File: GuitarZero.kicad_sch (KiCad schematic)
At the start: 16 parts, among them J1 USB_A, J2 USB_B_Micro, J3 AudioJack3_SwitchT, SW1 SW_Push, SW2 SW_Push, SW3 SW_Push, SW4 SW_Push, SW5 SW_Push, SW6 SW_Push

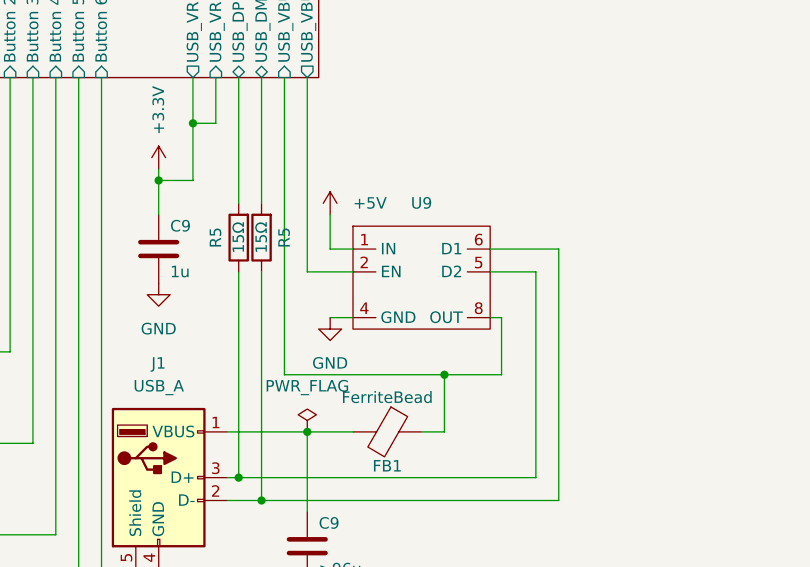
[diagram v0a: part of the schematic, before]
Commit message: Now follows with Electrical Rules
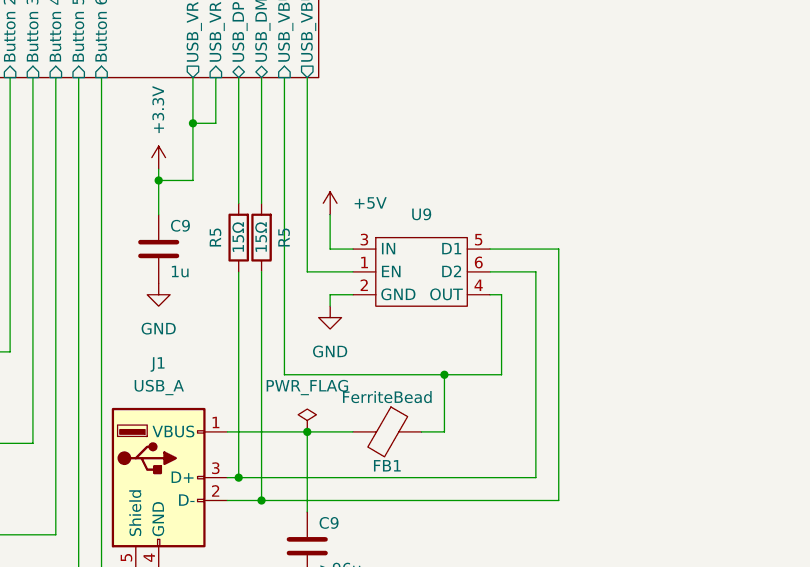
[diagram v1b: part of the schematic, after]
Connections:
- net +5V: now also U9.3 (IN); no longer U9.1 (IN)
- net GND: now also U9.2 (GND); no longer U9.4 (GND)
- net MCU/USB_VBUS: now also U9.4 (OUT); no longer U9.8 (OUT)
- net MCU/USB_VBUSEN: now also U9.1 (EN); no longer U9.2 (EN)
- net at J1.3 (D+), R5.1: now also U9.6 (D2); no longer U9.5 (D2)
- net at J1.2 (D-), R5.1: now also U9.5 (D1); no longer U9.6 (D1)

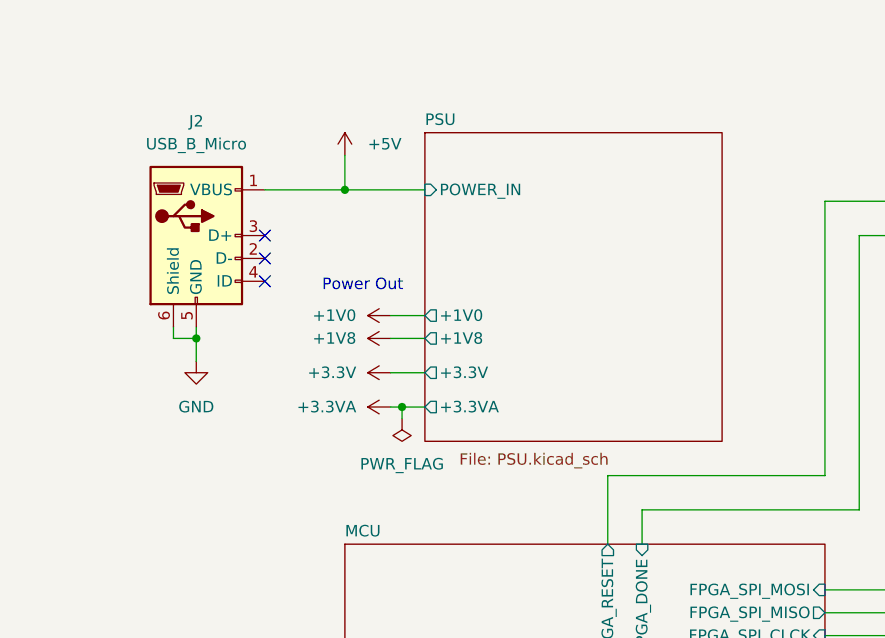
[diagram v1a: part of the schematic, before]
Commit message: Added PSU jumpers
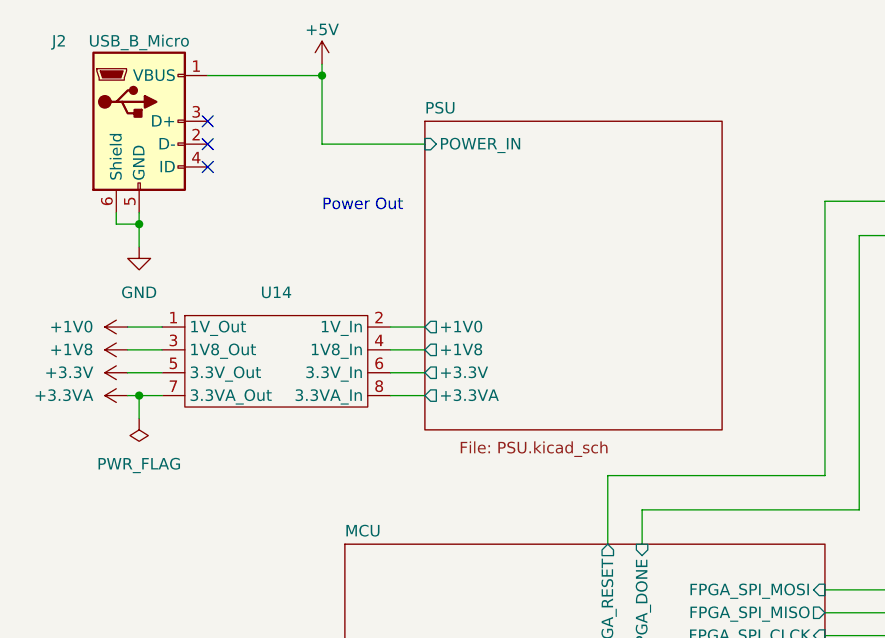
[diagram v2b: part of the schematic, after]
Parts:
- added U14: ~, symbol GuitarZero:PSU_Jumpers
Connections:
- net +1V0: now also U14.1 (1V_Out)
- net +1V8: now also U14.3 (1V8_Out)
- net +3.3V: now also U14.5 (3.3V_Out)
- net +3.3VA: now also U14.7 (3.3VA_Out)
- new net PSU/+1V0: U14.2 (1V_In)
- new net PSU/+1V8: U14.4 (1V8_In)
- new net PSU/+3.3V: U14.6 (3.3V_In)
- new net PSU/+3.3VA: U14.8 (3.3VA_In)
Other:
- moved on the sheet: J2

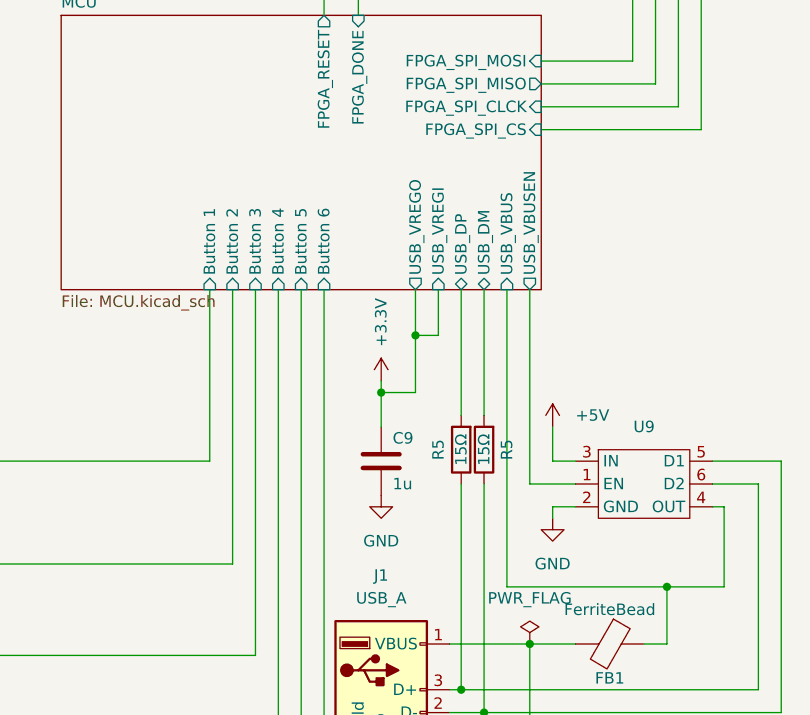
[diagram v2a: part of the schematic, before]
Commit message: Disconnected USB_VRGEI/O in root
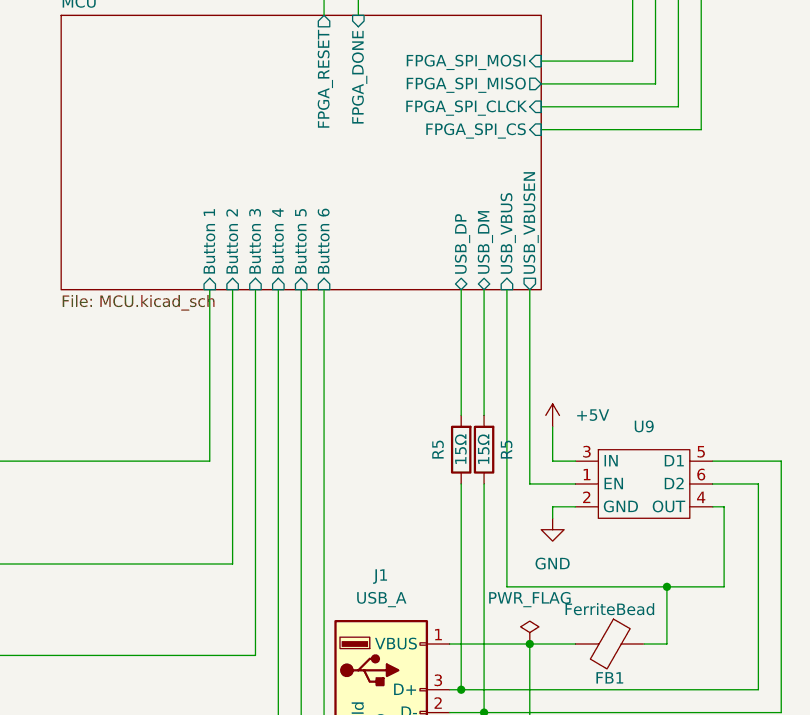
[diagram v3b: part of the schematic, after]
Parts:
- removed C9: 1u, symbol Device:C
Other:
- sheet MCU ports: added none; removed USB_VREGI, USB_VREGO
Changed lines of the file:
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@@
 (kicad_sch (version 20230121) (generator eeschema)
   (paper "A4")
-  (junction (at 82.55 113.03) (diameter 0) (color 0 0 0 0)
-  )
   (junction (at 232.41 25.4) (diameter 0) (color 0 0 0 0)
   )
@@
   )
   (junction (at 44.45 19.05) (diameter 0) (color 0 0 0 0)
-  )
-  (junction (at 86.36 106.68) (diameter 0) (color 0 0 0 0)
   )
   (junction (at 93.98 148.59) (diameter 0) (color 0 0 0 0)
@@
     (stroke (width 0) (type default))
   )
-  (wire (pts (xy 82.55 111.76) (xy 82.55 113.03))
-    (stroke (width 0) (type default))
-  )
   (wire (pts (xy 90.17 148.59) (xy 93.98 148.59))
     (stroke (width 0) (type default))
@@
     (stroke (width 0) (type default))
   )
-  (wire (pts (xy 86.36 101.6) (xy 86.36 106.68))
-    (stroke (width 0) (type default))
-  )
-  (wire (pts (xy 82.55 113.03) (xy 86.36 113.03))
-    (stroke (width 0) (type default))
-  )
   (wire (pts (xy 170.18 71.12) (xy 184.15 71.12))
     (stroke (width 0) (type default))
@@
     (stroke (width 0) (type default))
   )
-  (wire (pts (xy 86.36 106.68) (xy 88.9 106.68))
-    (stroke (width 0) (type default))
-  )
   (wire (pts (xy 237.49 25.4) (xy 232.41 25.4))
     (stroke (width 0) (type default))
@@
     (stroke (width 0) (type default))
   )
-  (wire (pts (xy 82.55 116.84) (xy 82.55 113.03))
-    (stroke (width 0) (type default))
-  )
   (wire (pts (xy 118.11 57.15) (xy 120.65 57.15))
     (stroke (width 0) (type default))
   )
-  (wire (pts (xy 86.36 113.03) (xy 86.36 106.68))
-    (stroke (width 0) (type default))
-  )
   (wire (pts (xy 24.13 142.24) (xy 27.94 142.24))
     (stroke (width 0) (type default))
@@
   )
   (wire (pts (xy 24.13 142.24) (xy 24.13 152.4))
-    (stroke (width 0) (type default))
-  )
-  (wire (pts (xy 88.9 101.6) (xy 88.9 106.68))
     (stroke (width 0) (type default))
   )
@@
         (path "/fba50eda-8593-4456-af98-ff56fd418a76"
           (reference "#PWR046") (unit 1)
-        )
-      )
-    )
-  )
-  (symbol (lib_id "power:+3.3V") (at 82.55 111.76 0) (unit 1)
-    (in_bom yes) (on_board yes) (dnp no)
-    (property "Reference" "#PWR051" (at 82.55 115.57 0)
-      (effects (font (size 1.27 1.27)) hide)
-    )
-    (property "Value" "+3.3V" (at 82.55 107.95 90)
-      (effects (font (size 1.27 1.27)) (justify left))
-    )
-    (property "Footprint" "" (at 82.55 111.76 0)
-      (effects (font (size 1.27 1.27)) hide)
-    )
-    (property "Datasheet" "" (at 82.55 111.76 0)
-      (effects (font (size 1.27 1.27)) hide)
-    )
-    (pin "1")
-    (instances
-      (project "GuitarZero"
-        (path "/fba50eda-8593-4456-af98-ff56fd418a76"
-          (reference "#PWR051") (unit 1)
         )
       )
@@
     )
   )
-  (symbol (lib_id "power:GND") (at 82.55 124.46 0) (unit 1)
-    (in_bom yes) (on_board yes) (dnp no)
-    (property "Reference" "#PWR050" (at 82.55 130.81 0)
-      (effects (font (size 1.27 1.27)) hide)
-    )
-    (property "Value" "GND" (at 82.55 129.54 0)
-      (effects (font (size 1.27 1.27)))
-    )
-    (property "Footprint" "" (at 82.55 124.46 0)
-      (effects (font (size 1.27 1.27)) hide)
-    )
-    (property "Datasheet" "" (at 82.55 124.46 0)
-      (effects (font (size 1.27 1.27)) hide)
-    )
-    (pin "1")
-    (instances
-      (project "GuitarZero"
-        (path "/fba50eda-8593-4456-af98-ff56fd418a76"
-          (reference "#PWR050") (unit 1)
-        )
-      )
-    )
-  )
   (symbol (lib_id "power:+3.3VA") (at 22.86 54.61 90) (unit 1)
     (in_bom yes) (on_board yes) (dnp no)
@@
         (path "/fba50eda-8593-4456-af98-ff56fd418a76"
           (reference "U9") (unit 1)
-        )
-      )
-    )
-  )
-  (symbol (lib_id "Device:C") (at 82.55 120.65 0) (unit 1)
-    (in_bom yes) (on_board yes) (dnp no)
-    (property "Reference" "C9" (at 83.82 118.11 0)
-      (effects (font (size 1.27 1.27)) (justify left))
-    )
-    (property "Value" "1u" (at 83.82 123.19 0)
-      (effects (font (size 1.27 1.27)) (justify left))
-    )
-    (property "Footprint" "" (at 83.5152 124.46 0)
-      (effects (font (size 1.27 1.27)) hide)
-    )
-    (property "Datasheet" "~" (at 82.55 120.65 0)
-      (effects (font (size 1.27 1.27)) hide)
-    )
-    (pin "1")
-    (pin "2")
-    (instances
-      (project "GuitarZero"
-        (path "/fba50eda-8593-4456-af98-ff56fd418a76/2f5e5303-1176-466f-800a-96bac7c62873"
-          (reference "C9") (unit 1)
-        )
-        (path "/fba50eda-8593-4456-af98-ff56fd418a76"
-          (reference "C71") (unit 1)
         )
       )
@@
       (effects (font (size 1.27 1.27)) (justify right))
     )
-    (pin "USB_VREGO" output (at 86.36 101.6 270)
-      (effects (font (size 1.27 1.27)) (justify left))
-    )
-    (pin "USB_VREGI" input (at 88.9 101.6 270)
-      (effects (font (size 1.27 1.27)) (justify left))
-    )
     (pin "USB_DP" bidirectional (at 91.44 101.6 270)

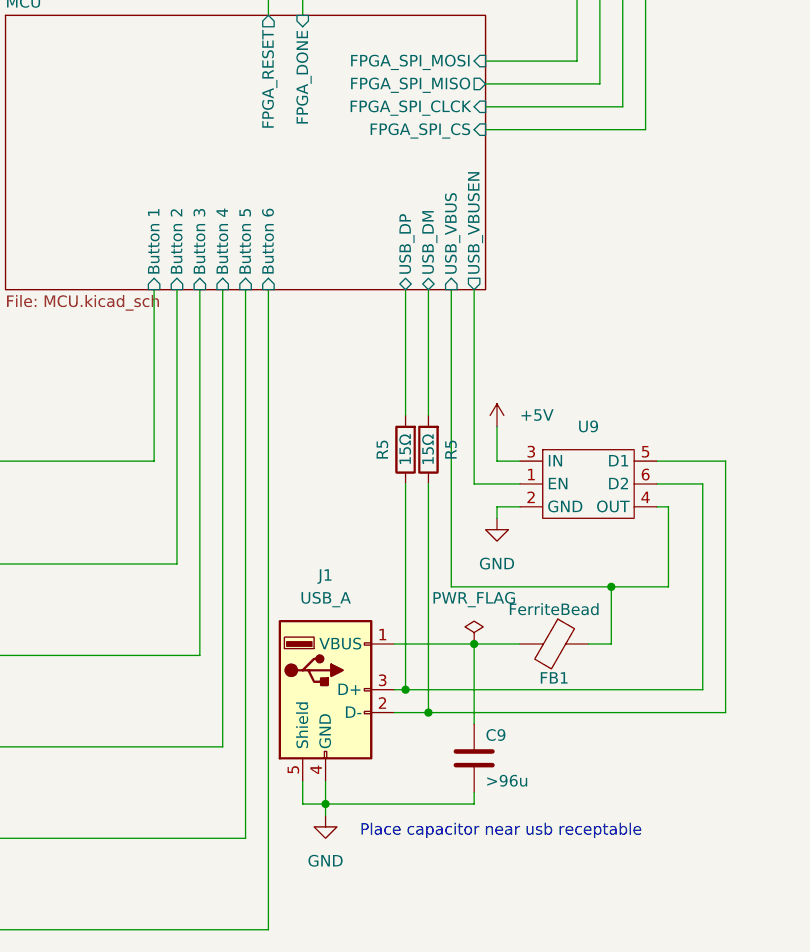
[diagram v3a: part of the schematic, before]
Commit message: Fixed mistake in USB_A connection
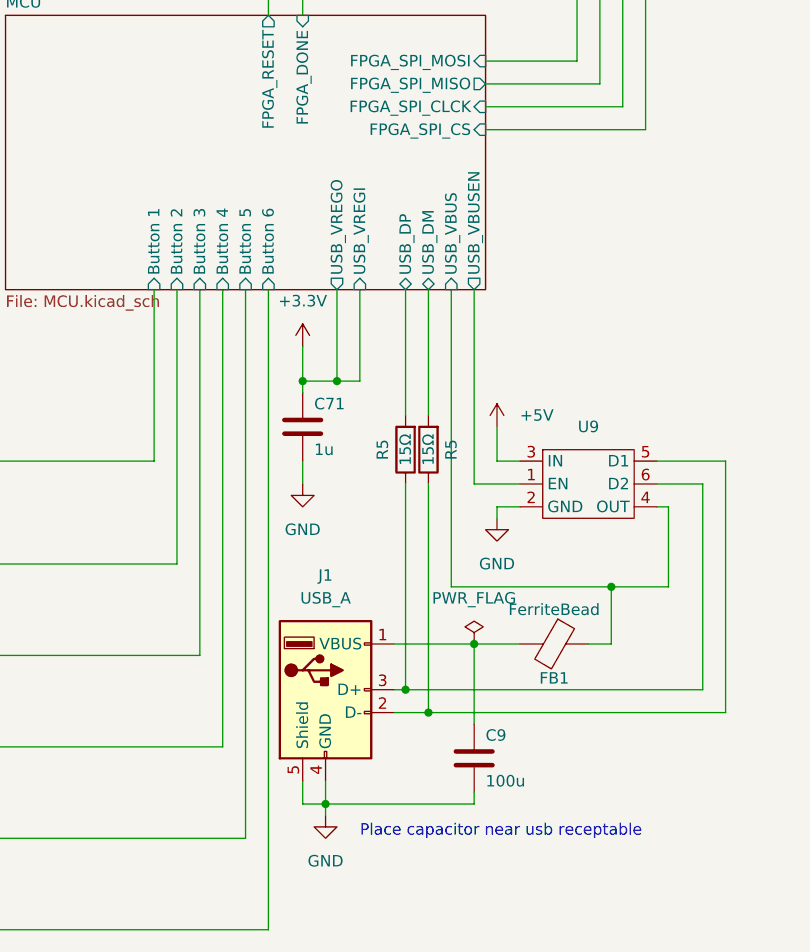
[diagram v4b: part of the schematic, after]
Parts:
- added C71: 1u, symbol Device:C
- C9: value >96u -> 100u
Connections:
- net +3.3V: now also C71.1
- net GND: now also C71.2
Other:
- sheet MCU ports: added USB_VREGI, USB_VREGO; removed none
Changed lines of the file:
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@@
   (junction (at 24.13 152.4) (diameter 0) (color 0 0 0 0)
+  )
+  (junction (at 80.01 111.76) (diameter 0) (color 0 0 0 0)
+  )
+  (junction (at 83.82 111.76) (diameter 0) (color 0 0 0 0)
   )
   (junction (at 24.13 54.61) (diameter 0) (color 0 0 0 0)
@@
     (stroke (width 0) (type default))
   )
+  (wire (pts (xy 80.01 120.65) (xy 80.01 123.19))
+    (stroke (width 0) (type default))
+  )
   (wire (pts (xy 91.44 146.05) (xy 91.44 123.19))
     (stroke (width 0) (type default))
@@
     (stroke (width 0) (type default))
   )
+  (wire (pts (xy 86.36 111.76) (xy 83.82 111.76))
+    (stroke (width 0) (type default))
+  )
   (wire (pts (xy 104.14 125.73) (xy 101.6 125.73))
     (stroke (width 0) (type default))
@@
     (stroke (width 0) (type default))
   )
+  (wire (pts (xy 80.01 111.76) (xy 83.82 111.76))
+    (stroke (width 0) (type default))
+  )
   (wire (pts (xy 24.13 38.1) (xy 24.13 35.56))
     (stroke (width 0) (type default))
@@
     (stroke (width 0) (type default))
   )
+  (wire (pts (xy 83.82 111.76) (xy 83.82 101.6))
+    (stroke (width 0) (type default))
+  )
   (wire (pts (xy 38.1 172.72) (xy 76.2 172.72))
     (stroke (width 0) (type default))
@@
     (stroke (width 0) (type default))
   )
+  (wire (pts (xy 80.01 107.95) (xy 80.01 111.76))
+    (stroke (width 0) (type default))
+  )
   (wire (pts (xy 104.14 67.31) (xy 104.14 36.83))
     (stroke (width 0) (type default))
@@
   )
   (wire (pts (xy 80.01 71.12) (xy 80.01 67.31))
+    (stroke (width 0) (type default))
+  )
+  (wire (pts (xy 80.01 111.76) (xy 80.01 113.03))
+    (stroke (width 0) (type default))
+  )
+  (wire (pts (xy 86.36 101.6) (xy 86.36 111.76))
     (stroke (width 0) (type default))
   )
@@
     )
   )
+  (symbol (lib_id "power:GND") (at 80.01 123.19 0) (unit 1)
+    (in_bom yes) (on_board yes) (dnp no)
+    (property "Reference" "#PWR051" (at 80.01 129.54 0)
+      (effects (font (size 1.27 1.27)) hide)
+    )
+    (property "Value" "GND" (at 80.01 128.27 0)
+      (effects (font (size 1.27 1.27)))
+    )
+    (property "Footprint" "" (at 80.01 123.19 0)
+      (effects (font (size 1.27 1.27)) hide)
+    )
+    (property "Datasheet" "" (at 80.01 123.19 0)
+      (effects (font (size 1.27 1.27)) hide)
+    )
+    (pin "1")
+    (instances
+      (project "GuitarZero"
+        (path "/fba50eda-8593-4456-af98-ff56fd418a76"
+          (reference "#PWR051") (unit 1)
+        )
+      )
+    )
+  )
+  (symbol (lib_id "Device:C") (at 80.01 116.84 0) (unit 1)
+    (in_bom yes) (on_board yes) (dnp no)
+    (property "Reference" "C71" (at 81.28 114.3 0)
+      (effects (font (size 1.27 1.27)) (justify left))
+    )
+    (property "Value" "1u" (at 81.28 119.38 0)
+      (effects (font (size 1.27 1.27)) (justify left))
+    )
+    (property "Footprint" "" (at 80.9752 120.65 0)
+      (effects (font (size 1.27 1.27)) hide)
+    )
+    (property "Datasheet" "~" (at 80.01 116.84 0)
+      (effects (font (size 1.27 1.27)) hide)
+    )
+    (pin "1")
+    (pin "2")
+    (instances
+      (project "GuitarZero"
+        (path "/fba50eda-8593-4456-af98-ff56fd418a76"
+          (reference "C71") (unit 1)
+        )
+      )
+    )
+  )
+  (symbol (lib_id "power:+3.3V") (at 80.01 107.95 0) (unit 1)
+    (in_bom yes) (on_board yes) (dnp no) (fields_autoplaced)
+    (property "Reference" "#PWR050" (at 80.01 111.76 0)
+      (effects (font (size 1.27 1.27)) hide)
+    )
+    (property "Value" "+3.3V" (at 80.01 102.87 0)
+      (effects (font (size 1.27 1.27)))
+    )
+    (property "Footprint" "" (at 80.01 107.95 0)
+      (effects (font (size 1.27 1.27)) hide)
+    )
+    (property "Datasheet" "" (at 80.01 107.95 0)
+      (effects (font (size 1.27 1.27)) hide)
+    )
+    (pin "1")
+    (instances
+      (project "GuitarZero"
+        (path "/fba50eda-8593-4456-af98-ff56fd418a76"
+          (reference "#PWR050") (unit 1)
+        )
+      )
+    )
+  )
   (symbol (lib_id "Device:C") (at 99.06 153.67 0) (unit 1)
     (in_bom yes) (on_board yes) (dnp no)
@@
       (effects (font (size 1.27 1.27)) (justify left))
     )
-    (property "Value" ">96u" (at 100.33 156.21 0)
+    (property "Value" "100u" (at 100.33 156.21 0)
       (effects (font (size 1.27 1.27)) (justify left))
     )
@@
       (effects (font (size 1.27 1.27)) (justify left))
     )
+    (pin "USB_VREGI" input (at 86.36 101.6 270)
+      (effects (font (size 1.27 1.27)) (justify left))
+    )
+    (pin "USB_VREGO" output (at 83.82 101.6 270)
+      (effects (font (size 1.27 1.27)) (justify left))
+    )

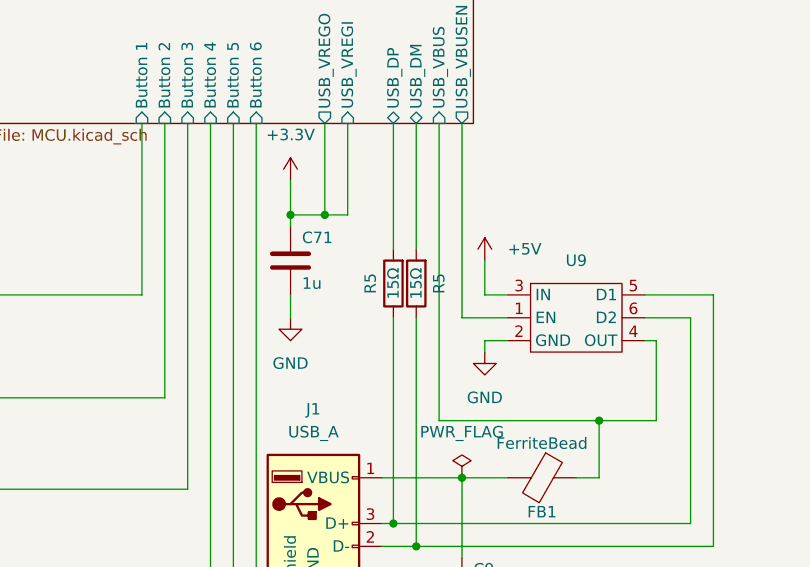
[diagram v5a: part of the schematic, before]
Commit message: Made resistor values uniform
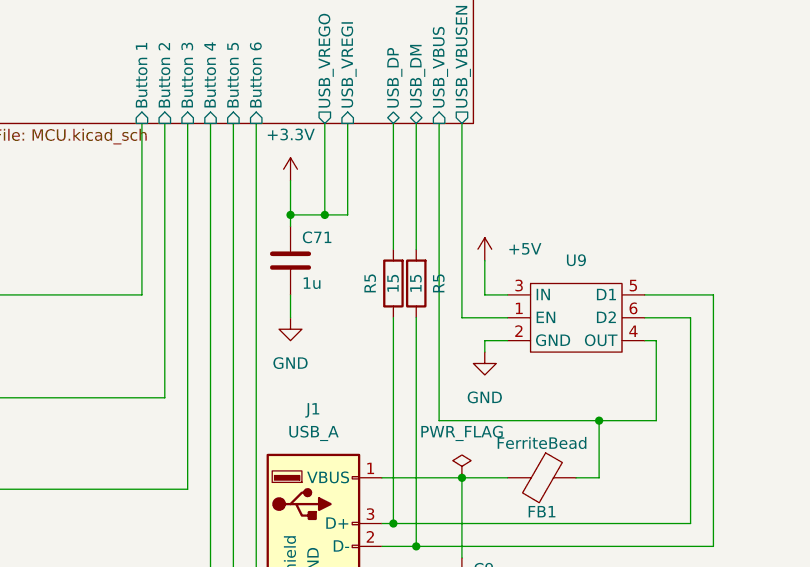
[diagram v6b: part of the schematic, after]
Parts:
- R5: value 15Ω -> 15
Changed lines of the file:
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@@
       (effects (font (size 1.27 1.27)))
     )
-    (property "Value" "15Ω" (at 91.44 119.38 90)
+    (property "Value" "15" (at 91.44 119.38 90)
       (effects (font (size 1.27 1.27)))
     )
@@
       (effects (font (size 1.27 1.27)))
     )
-    (property "Value" "15Ω" (at 93.98 119.38 90)
+    (property "Value" "15" (at 93.98 119.38 90)
       (effects (font (size 1.27 1.27)))
     )
